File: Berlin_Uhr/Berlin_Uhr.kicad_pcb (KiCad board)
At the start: 2 copper layers, 100 x 130.1 mm, 56 parts, among them J1 USB_C_Receptacle_USB2.0, J2 ISP, Q1 KPS-3227, SW1 SW_Push, SW2 SW_Push, U1 DS3231M, U2 ATtiny167-SU, U3 TLC5947DAP, Y1 16MHz

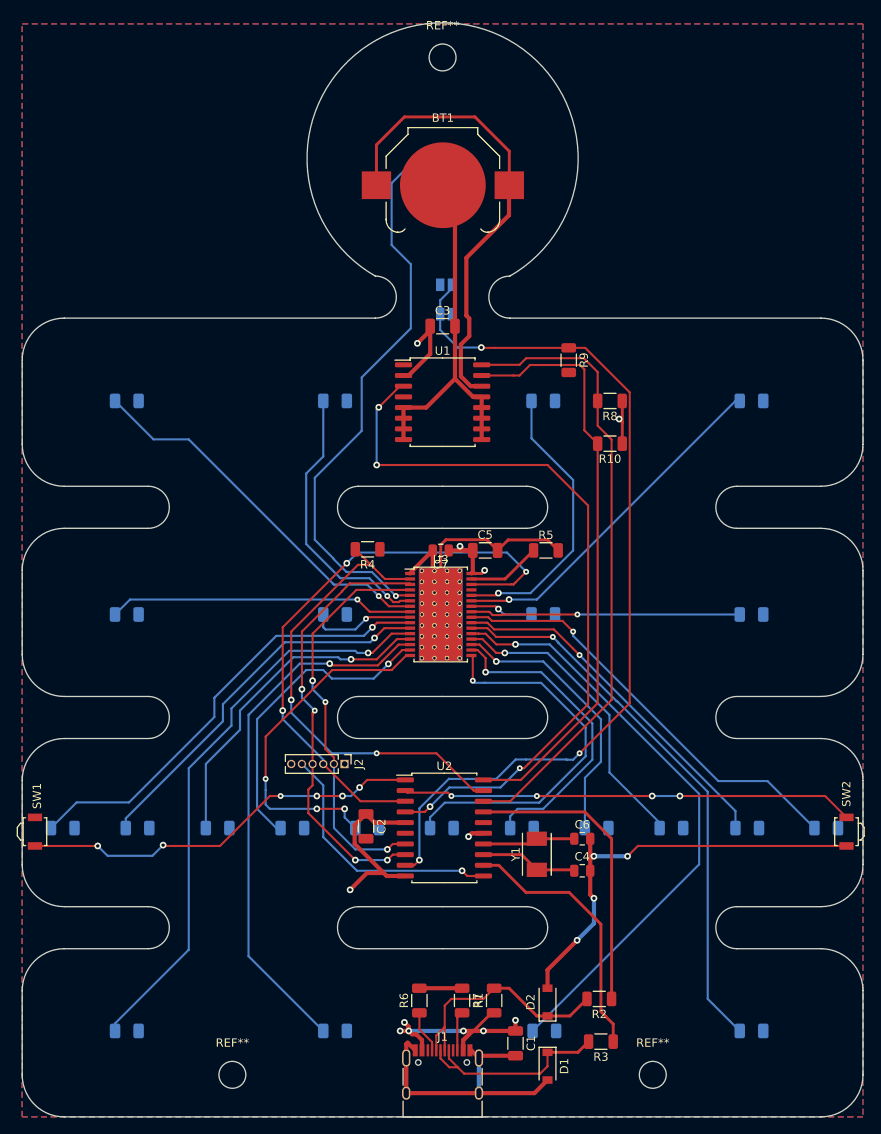
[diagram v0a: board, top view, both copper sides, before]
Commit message: LED Frame added
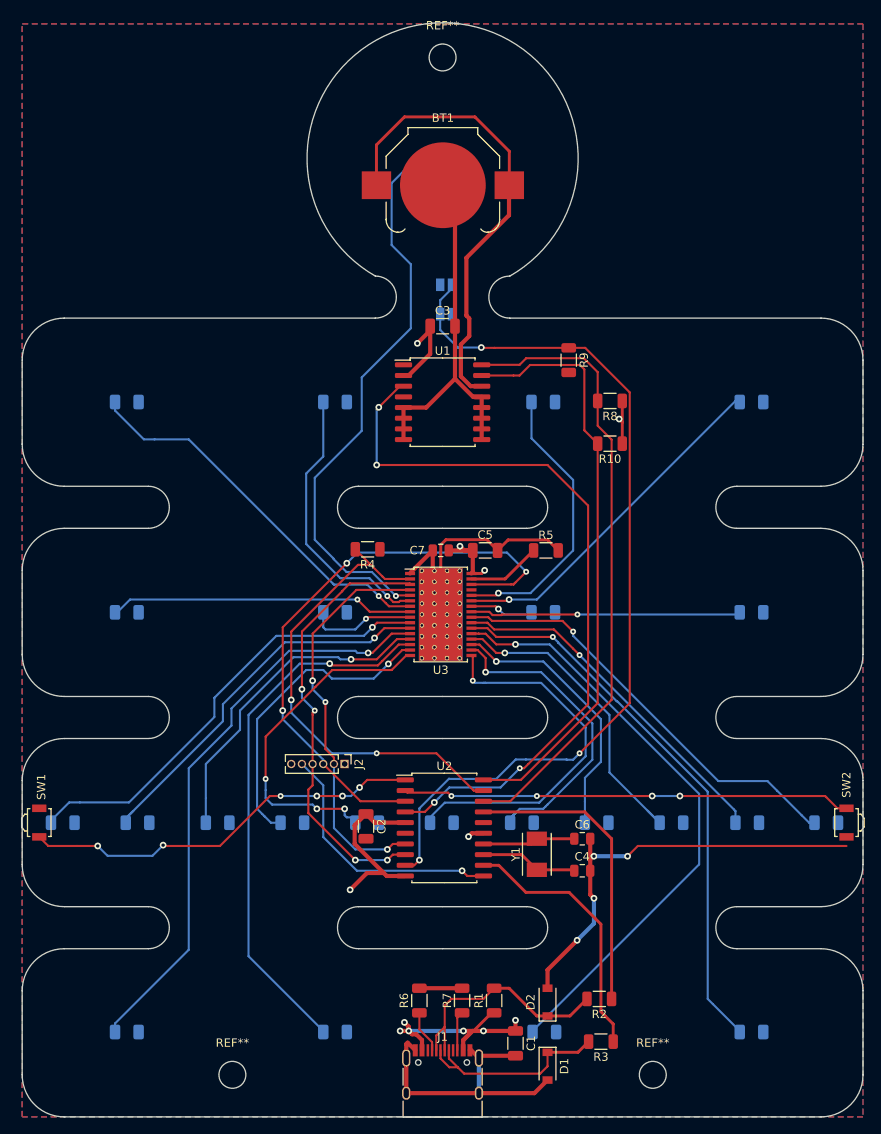
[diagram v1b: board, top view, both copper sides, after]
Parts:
- added G***: Berlin Clock LED Frame, mystuff:LED-Frame, B.Cu at (145.0, 90.0)
- moved SW1 1.19 mm to (97.0, 120.0)
- moved SW2 1.08 mm to (193.0, 120.0)
- moved D11 0.64 mm to (118.2, 120.0)
- moved D13 0.64 mm to (127.1, 120.0)
- moved D14 0.64 mm to (136.0, 120.0)
- moved D15 0.64 mm to (144.9, 120.0)
- moved D16 0.64 mm to (154.4, 120.0)
- moved D17 0.64 mm to (163.3, 120.0)
- moved D18 0.64 mm to (172.2, 120.0)
- moved D21 0.64 mm to (181.2, 120.0)
- moved D22 0.64 mm to (190.6, 120.0)
- moved D8 0.64 mm to (99.8, 120.0)
- moved D9 0.64 mm to (108.7, 120.0)
- moved D3 0.38 mm to (144.9, 41.0)
- moved D23 0.25 mm to (181.7, 95.0)
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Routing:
- net Net-(D16-Pad1): track 37.3 -> 38.8 mm
- net Net-(D17-Pad1): track 32.8 -> 31.5 mm
- net Net-(D15-Pad1): track 45.3 -> 44.0 mm
- net Net-(D11-Pad1): track 39.6 -> 38.3 mm
- net Net-(D14-Pad1): track 41.7 -> 40.5 mm
- net Net-(D18-Pad1): track 36.1 -> 37.2 mm
- net Net-(D21-Pad1): track 42.7 -> 42.1 mm
- net Net-(D5-Pad1): track 45.2 -> 45.7 mm
- net Net-(D8-Pad1): track 54.2 -> 53.6 mm
